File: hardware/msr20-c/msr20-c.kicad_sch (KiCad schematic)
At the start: 10 parts, among them J2 TO OLED, J3 TO ENCODER, J4 SWD, J5 AUDIO OUT, U5 Pico

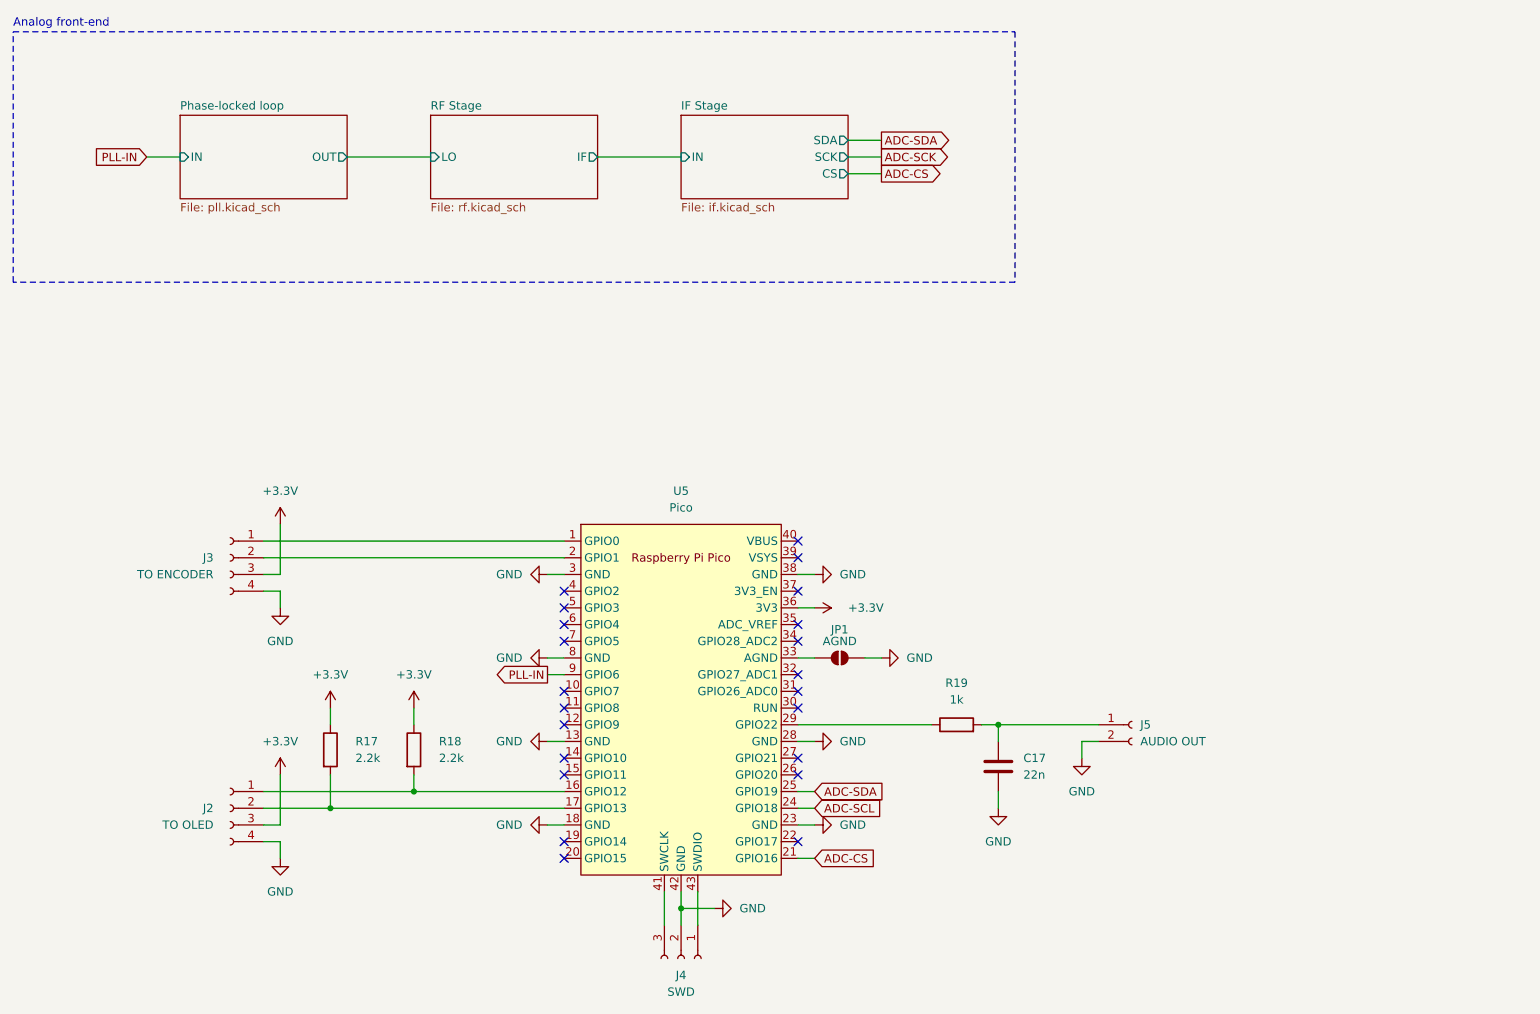
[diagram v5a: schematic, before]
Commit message: add power sheet, assign footprints
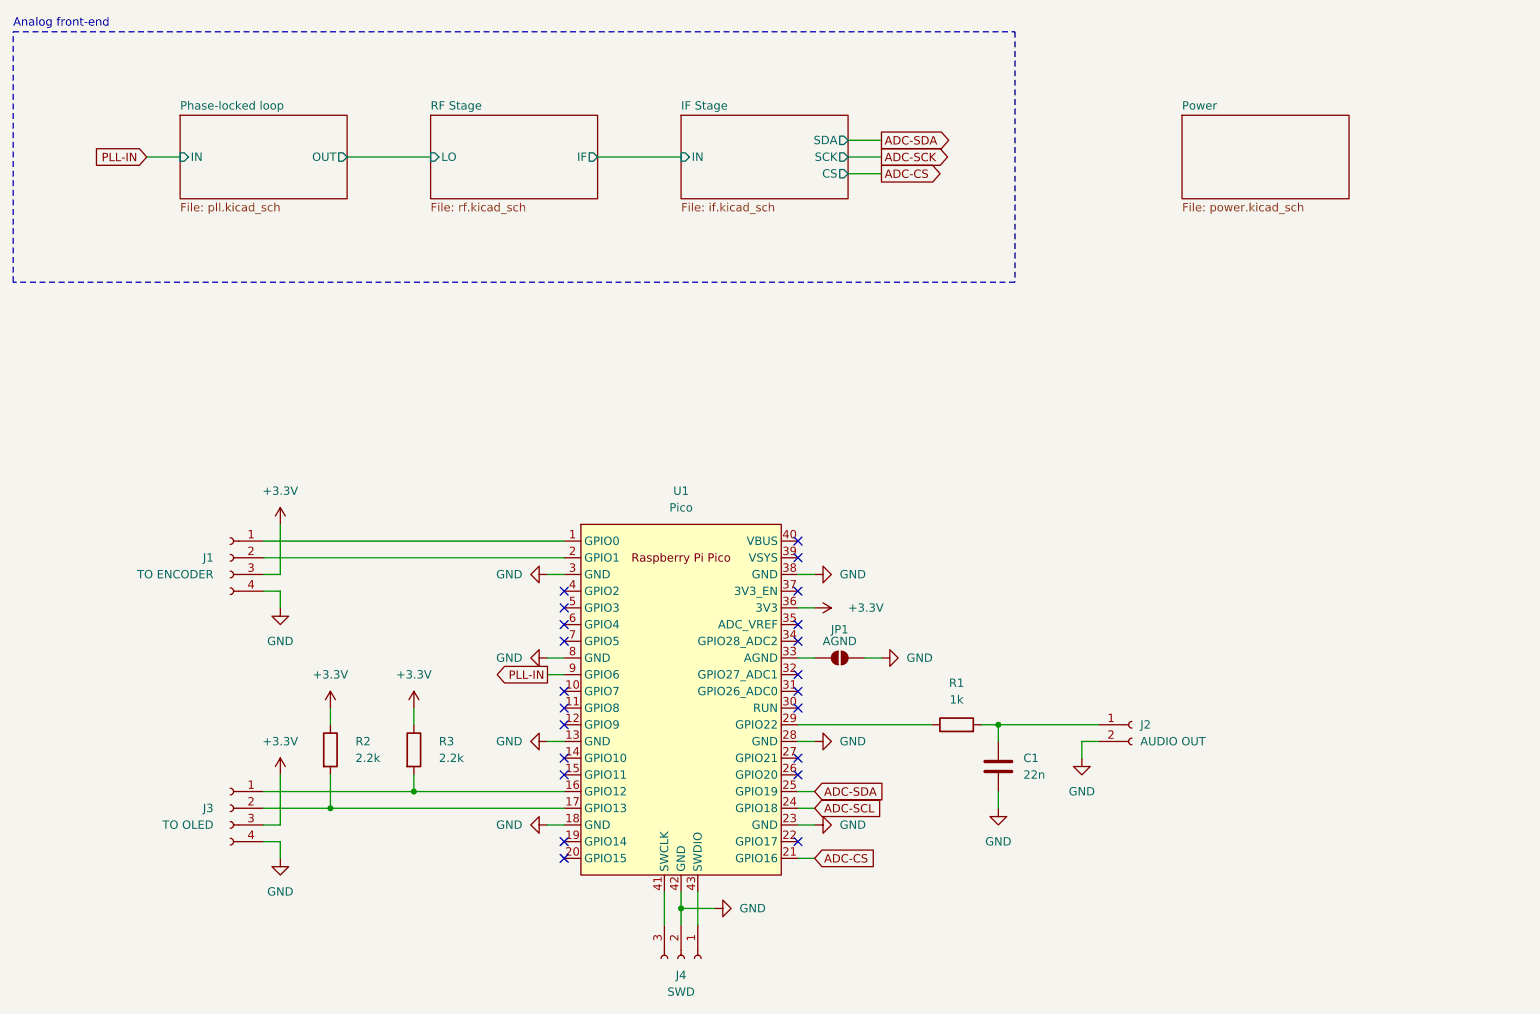
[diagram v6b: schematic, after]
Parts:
- C1: renamed from C17; footprint (none) -> Capacitor_SMD:C_0805_2012Metric
- J1: renamed from J3; footprint (none) -> Connector_PinHeader_2.54mm:PinHeader_1x04_P2.54mm_Horizontal
- J2: renamed from J5; footprint (none) -> Connector_PinHeader_2.54mm:PinHeader_1x02_P2.54mm_Horizontal
- J3: renamed from J2; footprint (none) -> Connector_PinHeader_2.54mm:PinHeader_1x04_P2.54mm_Horizontal
- J4: footprint (none) -> Connector_PinHeader_2.54mm:PinHeader_1x03_P2.54mm_Horizontal
- JP1: footprint (none) -> Jumper:SolderJumper-2_P1.3mm_Bridged_Pad1.0x1.5mm
- R1: renamed from R19; footprint (none) -> Resistor_SMD:R_0805_2012Metric
- R2: renamed from R17; footprint (none) -> Resistor_SMD:R_0805_2012Metric
- R3: renamed from R18; footprint (none) -> Resistor_SMD:R_0805_2012Metric
- renumbered U5 to U1
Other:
- added sheet Power (power.kicad_sch)
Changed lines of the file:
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@@
 		(dnp no)
 		(fields_autoplaced yes)
-		(property "Reference" "#PWR048"
+		(property "Reference" "#PWR017"
 			(at 66.04 157.48 0)
 			(effects
@@
 			(project "msr20-c"
 				(path "/3d24e86e-b070-4f0e-8c28-04e9dd9d95d1"
-					(reference "#PWR048")
+					(reference "#PWR017")
 					(unit 1)
 				)
@@
 		(dnp no)
 		(fields_autoplaced yes)
-		(property "Reference" "#PWR050"
+		(property "Reference" "#PWR01"
 			(at 66.04 104.14 0)
 			(effects
@@
 			(project "msr20-c"
 				(path "/3d24e86e-b070-4f0e-8c28-04e9dd9d95d1"
-					(reference "#PWR050")
+					(reference "#PWR01")
 					(unit 1)
 				)
@@
 		(dnp no)
 		(fields_autoplaced yes)
-		(property "Reference" "R19"
+		(property "Reference" "R1"
 			(at 168.91 124.46 90)
 			(effects
@@
 			)
 		)
-		(property "Footprint" ""
+		(property "Footprint" "Resistor_SMD:R_0805_2012Metric"
 			(at 168.91 132.588 90)
 			(effects
@@
 			(project "msr20-c"
 				(path "/3d24e86e-b070-4f0e-8c28-04e9dd9d95d1"
-					(reference "R19")
+					(reference "R1")
 					(unit 1)
 				)
@@
 		(dnp no)
 		(fields_autoplaced yes)
-		(property "Reference" "C17"
+		(property "Reference" "C1"
 			(at 179.07 135.8899 0)
 			(effects
@@
 			)
 		)
-		(property "Footprint" ""
+		(property "Footprint" "Capacitor_SMD:C_0805_2012Metric"
 			(at 176.2252 140.97 0)
 			(effects
@@
 			(project "msr20-c"
 				(path "/3d24e86e-b070-4f0e-8c28-04e9dd9d95d1"
-					(reference "C17")
+					(reference "C1")
 					(unit 1)
 				)
@@
 		(on_board yes)
 		(dnp no)
-		(property "Reference" "J3"
+		(property "Reference" "J1"
 			(at 55.88 105.4099 0)
 			(effects
@@
 			)
 		)
-		(property "Footprint" ""
+		(property "Footprint" "Connector_PinHeader_2.54mm:PinHeader_1x04_P2.54mm_Horizontal"
 			(at 58.42 105.41 0)
 			(effects
@@
 			(project "msr20-c"
 				(path "/3d24e86e-b070-4f0e-8c28-04e9dd9d95d1"
-					(reference "J3")
+					(reference "J1")
 					(unit 1)
 				)
@@
 		(dnp no)
 		(fields_autoplaced yes)
-		(property "Reference" "#PWR043"
+		(property "Reference" "#PWR015"
 			(at 100.33 146.05 0)
 			(effects
@@
 			(project "msr20-c"
 				(path "/3d24e86e-b070-4f0e-8c28-04e9dd9d95d1"
-					(reference "#PWR043")
+					(reference "#PWR015")
 					(unit 1)
 				)
@@
 		(on_board yes)
 		(dnp no)
-		(property "Reference" "J2"
+		(property "Reference" "J3"
 			(at 55.88 143.5099 0)
 			(effects
@@
 			)
 		)
-		(property "Footprint" ""
+		(property "Footprint" "Connector_PinHeader_2.54mm:PinHeader_1x04_P2.54mm_Horizontal"
 			(at 58.42 143.51 0)
 			(effects
@@
 			(project "msr20-c"
 				(path "/3d24e86e-b070-4f0e-8c28-04e9dd9d95d1"
-					(reference "J2")
+					(reference "J3")
 					(unit 1)
 				)
@@
 		(dnp no)
 		(fields_autoplaced yes)
-		(property "Reference" "#PWR051"
+		(property "Reference" "#PWR04"
 			(at 66.04 119.38 0)
 			(effects
@@
 			(project "msr20-c"
 				(path "/3d24e86e-b070-4f0e-8c28-04e9dd9d95d1"
-					(reference "#PWR051")
+					(reference "#PWR04")
 					(unit 1)
 				)
@@
 		(dnp no)
 		(fields_autoplaced yes)
-		(property "Reference" "#PWR042"
+		(property "Reference" "#PWR010"
 			(at 100.33 133.35 0)
 			(effects
@@
 			(project "msr20-c"
 				(path "/3d24e86e-b070-4f0e-8c28-04e9dd9d95d1"
-					(reference "#PWR042")
+					(reference "#PWR010")
 					(unit 1)
 				)
@@
 		(dnp no)
 		(fields_autoplaced yes)
-		(property "Reference" "#PWR046"
+		(property "Reference" "#PWR09"
 			(at 86.36 132.08 0)
 			(effects
@@
 			(project "msr20-c"
 				(path "/3d24e86e-b070-4f0e-8c28-04e9dd9d95d1"
-					(reference "#PWR046")
+					(reference "#PWR09")
 					(unit 1)
 				)
@@
 		(dnp no)
 		(fields_autoplaced yes)
-		(property "Reference" "#PWR039"
+		(property "Reference" "#PWR011"
 			(at 153.67 133.35 0)
 			(effects
@@
 			(project "msr20-c"
 				(path "/3d24e86e-b070-4f0e-8c28-04e9dd9d95d1"
-					(reference "#PWR039")
+					(reference "#PWR011")
 					(unit 1)
 				)
@@
 			)
 		)
-		(property "Footprint" ""
+		(property "Footprint" "Jumper:SolderJumper-2_P1.3mm_Bridged_Pad1.0x1.5mm"
 			(at 151.13 120.65 0)
 			(effects
@@
 		(dnp no)
 		(fields_autoplaced yes)
-		(property "Reference" "#PWR053"
+		(property "Reference" "#PWR012"
 			(at 187.96 142.24 0)
 			(effects
@@
 			(project "msr20-c"
 				(path "/3d24e86e-b070-4f0e-8c28-04e9dd9d95d1"
-					(reference "#PWR053")
+					(reference "#PWR012")
 					(unit 1)
 				)
@@
 		(dnp no)
 		(fields_autoplaced yes)
-		(property "Reference" "#PWR045"
+		(property "Reference" "#PWR05"
 			(at 143.51 113.03 0)
 			(effects
@@
 			(project "msr20-c"
 				(path "/3d24e86e-b070-4f0e-8c28-04e9dd9d95d1"
-					(reference "#PWR045")
+					(reference "#PWR05")
 					(unit 1)
 				)
@@
 		(dnp no)
 		(fields_autoplaced yes)
-		(property "Reference" "#PWR037"
+		(property "Reference" "#PWR03"
 			(at 153.67 107.95 0)
 			(effects
@@
 			(project "msr20-c"
 				(path "/3d24e86e-b070-4f0e-8c28-04e9dd9d95d1"
-					(reference "#PWR037")
+					(reference "#PWR03")
 					(unit 1)
 				)
@@
 		(dnp no)
 		(fields_autoplaced yes)
-		(property "Reference" "#PWR040"
+		(property "Reference" "#PWR02"
 			(at 100.33 107.95 0)
 			(effects
@@
 			(project "msr20-c"
 				(path "/3d24e86e-b070-4f0e-8c28-04e9dd9d95d1"
-					(reference "#PWR040")
+					(reference "#PWR02")
 					(unit 1)
 				)
@@
 		(dnp no)
 		(fields_autoplaced yes)
-		(property "Reference" "R18"
+		(property "Reference" "R3"
 			(at 90.17 133.3499 0)
 			(effects
@@
 			)
 		)
-		(property "Footprint" ""
+		(property "Footprint" "Resistor_SMD:R_0805_2012Metric"
 			(at 84.582 134.62 90)
 			(effects
@@
 			(project "msr20-c"
 				(path "/3d24e86e-b070-4f0e-8c28-04e9dd9d95d1"
-					(reference "R18")
+					(reference "R3")
 					(unit 1)
 				)
@@
 		(dnp no)
 		(fields_autoplaced yes)
-		(property "Reference" "R17"
+		(property "Reference" "R2"
 			(at 77.47 133.3499 0)
 			(effects
@@
 			)
 		)
-		(property "Footprint" ""
+		(property "Footprint" "Resistor_SMD:R_0805_2012Metric"
 			(at 71.882 134.62 90)
 			(effects
@@
 			(project "msr20-c"
 				(path "/3d24e86e-b070-4f0e-8c28-04e9dd9d95d1"
-					(reference "R17")
+					(reference "R2")
 					(unit 1)
 				)
@@
 		(dnp no)
 		(fields_autoplaced yes)
-		(property "Reference" "U5"
+		(property "Reference" "U1"
 			(at 127 95.25 0)
 			(effects
@@
 			(project "msr20-c"
 				(path "/3d24e86e-b070-4f0e-8c28-04e9dd9d95d1"
-					(reference "U5")
+					(reference "U1")
 					(unit 1)
 				)
@@
 		(dnp no)
 		(fields_autoplaced yes)
-		(property "Reference" "#PWR038"
+		(property "Reference" "#PWR016"
 			(at 153.67 146.05 0)
 			(effects
@@
 			(project "msr20-c"
 				(path "/3d24e86e-b070-4f0e-8c28-04e9dd9d95d1"
-					(reference "#PWR038")
+					(reference "#PWR016")
 					(unit 1)
 				)
@@
 		(dnp no)
 		(fields_autoplaced yes)
-		(property "Reference" "#PWR047"
+		(property "Reference" "#PWR08"
 			(at 73.66 132.08 0)
 			(effects
@@
 			(project "msr20-c"
 				(path "/3d24e86e-b070-4f0e-8c28-04e9dd9d95d1"
-					(reference "#PWR047")
+					(reference "#PWR08")
 					(unit 1)
 				)
@@
 		(dnp no)
 		(fields_autoplaced yes)
-		(property "Reference" "#PWR036"
+		(property "Reference" "#PWR07"
 			(at 163.83 120.65 0)
 			(effects
@@
 			(project "msr20-c"
 				(path "/3d24e86e-b070-4f0e-8c28-04e9dd9d95d1"
-					(reference "#PWR036")
+					(reference "#PWR07")
 					(unit 1)
 				)
@@
 		(dnp no)
 		(fields_autoplaced yes)
-		(property "Reference" "#PWR052"
+		(property "Reference" "#PWR014"
 			(at 175.26 149.86 0)
 			(effects
@@
 			(project "msr20-c"
 				(path "/3d24e86e-b070-4f0e-8c28-04e9dd9d95d1"
-					(reference "#PWR052")
+					(reference "#PWR014")
 					(unit 1)
 				)
@@
 			)
 		)
-		(property "Footprint" ""
+		(property "Footprint" "Connector_PinHeader_2.54mm:PinHeader_1x03_P2.54mm_Horizontal"
 			(at 127 166.37 0)
 			(effects
@@
 		(dnp no)
 		(fields_autoplaced yes)
-		(property "Reference" "#PWR044"
+		(property "Reference" "#PWR018"
 			(at 138.43 158.75 0)
 			(effects
@@
 			(project "msr20-c"
 				(path "/3d24e86e-b070-4f0e-8c28-04e9dd9d95d1"
-					(reference "#PWR044")
+					(reference "#PWR018")
 					(unit 1)
 				)
@@
 		(dnp no)
 		(fields_autoplaced yes)
-		(property "Reference" "#PWR049"
+		(property "Reference" "#PWR013"
 			(at 66.04 142.24 0)
 			(effects
@@
 			(project "msr20-c"
 				(path "/3d24e86e-b070-4f0e-8c28-04e9dd9d95d1"
-					(reference "#PWR049")
+					(reference "#PWR013")
 					(unit 1)
 				)
@@
 		(dnp no)
 		(fields_autoplaced yes)
-		(property "Reference" "#PWR041"
+		(property "Reference" "#PWR06"
 			(at 100.33 120.65 0)
 			(effects
@@
 			(project "msr20-c"
 				(path "/3d24e86e-b070-4f0e-8c28-04e9dd9d95d1"
-					(reference "#PWR041")
+					(reference "#PWR06")
 					(unit 1)
 				)
@@
 		(dnp no)
 		(fields_autoplaced yes)
-		(property "Reference" "J5"
+		(property "Reference" "J2"
 			(at 196.85 130.8099 0)
 			(effects
@@
 			)
 		)
-		(property "Footprint" ""
+		(property "Footprint" "Connector_PinHeader_2.54mm:PinHeader_1x02_P2.54mm_Horizontal"
 			(at 195.58 130.81 0)
 			(effects
@@
 			(project "msr20-c"
 				(path "/3d24e86e-b070-4f0e-8c28-04e9dd9d95d1"
-					(reference "J5")
+					(reference "J2")
 					(unit 1)
 				)
@@
 				)
 			)
+		)
+	)
+	(sheet
+		(at 203.2 38.1)
+		(size 25.4 12.7)
+		(fields_autoplaced yes)
+		(stroke
+			(width 0.1524)
+			(type solid)
+		)
+		(fill
+			(color 0 0 0 0.0000)
+		)
+		(property "Sheetname" "Power"
+			(at 203.2 37.3884 0)
+			(effects
+				(font
+					(size 1.27 1.27)
+				)
+				(justify left bottom)
+			)
+		)
+		(property "Sheetfile" "power.kicad_sch"
+			(at 203.2 51.3846 0)
+			(effects
+				(font
+					(size 1.27 1.27)
+				)
+				(justify left top)
+			)
+		)
+		(instances
+			(project "msr20-c"
+				(path "/3d24e86e-b070-4f0e-8c28-04e9dd9d95d1"
+					(page "5")
+				)
+			)

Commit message: pcb: pll, lna, rf-bpf layout
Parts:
- J1, J3: footprint Connector_PinHeader_2.54mm:PinHeader_1x04_P2.54mm_Horizontal -> Connector_PinHeader_2.54mm:PinHeader_1x04_P2.54mm_Vertical
- J2: footprint Connector_PinHeader_2.54mm:PinHeader_1x02_P2.54mm_Horizontal -> Connector_PinHeader_2.54mm:PinHeader_1x02_P2.54mm_Vertical
- J4: footprint Connector_PinHeader_2.54mm:PinHeader_1x03_P2.54mm_Horizontal -> Connector_PinHeader_2.54mm:PinHeader_1x03_P2.54mm_Vertical
- U1: footprint RPi_Pico:RPi_Pico_SMD_TH -> MCU_RaspberryPi_and_Boards:RPi_Pico_SMD_TH
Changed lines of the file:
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@@
 			)
 		)
-		(property "Footprint" "Connector_PinHeader_2.54mm:PinHeader_1x04_P2.54mm_Horizontal"
+		(property "Footprint" "Connector_PinHeader_2.54mm:PinHeader_1x04_P2.54mm_Vertical"
 			(at 58.42 105.41 0)
 			(effects
@@
 			)
 		)
-		(property "Footprint" "Connector_PinHeader_2.54mm:PinHeader_1x04_P2.54mm_Horizontal"
+		(property "Footprint" "Connector_PinHeader_2.54mm:PinHeader_1x04_P2.54mm_Vertical"
 			(at 58.42 143.51 0)
 			(effects
@@
 			)
 		)
-		(property "Footprint" "RPi_Pico:RPi_Pico_SMD_TH"
+		(property "Footprint" "MCU_RaspberryPi_and_Boards:RPi_Pico_SMD_TH"
 			(at 127 127 90)
 			(effects
@@
 			)
 		)
-		(property "Footprint" "Connector_PinHeader_2.54mm:PinHeader_1x03_P2.54mm_Horizontal"
+		(property "Footprint" "Connector_PinHeader_2.54mm:PinHeader_1x03_P2.54mm_Vertical"
 			(at 127 166.37 0)
 			(effects
@@
 			)
 		)
-		(property "Footprint" "Connector_PinHeader_2.54mm:PinHeader_1x02_P2.54mm_Horizontal"
+		(property "Footprint" "Connector_PinHeader_2.54mm:PinHeader_1x02_P2.54mm_Vertical"
 			(at 195.58 130.81 0)
 			(effects

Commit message: finish pcb rev 1, new png render
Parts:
- added H1, H2, H3, H4: MountingHole_Pad, MountingHole:MountingHole_3.2mm_M3_DIN965_Pad_TopBottom, symbol Mechanical:MountingHole_Pad
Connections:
- net ADC-SCL is gone; now on net ADC-SCK: U1.24 (GPIO18)
- net GND: now also H1.1, H2.1, H3.1, H4.1
- net PLL-IN: now also U1.31 (GPIO26_ADC0); no longer U1.9 (GPIO6)
